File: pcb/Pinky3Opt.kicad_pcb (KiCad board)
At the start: 2 copper layers, 136 x 102.7 mm, 74 parts, among them J1 USB_C_Receptacle_USB2.0, J2 Conn_01x04, SW1 Reset, U1 ATmega32U4-A, U2 PRTR5V0U2X, Y1 16MHz

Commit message: through hole
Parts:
- added ?: Val**, kbd:M2_HOLE_v2, F.Cu at (47.6, 73.8)
- added ?: Val**, kbd:M2_HOLE_v2, F.Cu at (133.3, 92.0)
- added ?: Val**, kbd:M2_HOLE_v2, F.Cu at (47.6, 54.8)
- added Ref**: Val**, kbd:M2_HOLE_v2, F.Cu at (142.9, 50.0)
- moved D7 5.78 mm to (141.2, 43.5)
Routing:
- net /L_ROW0: track 178.2 -> 179.3 mm
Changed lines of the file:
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@@
       (net 31 "Net-(D22-A)") (pinfunction "ROW") (pintype "passive"))
   )
+  (footprint "kbd:M2_HOLE_v2" (layer "F.Cu")
+    (at 142.875 50)
+    (descr "Mounting Hole 2.2mm, no annular, M2")
+    (tags "mounting hole 2.2mm no annular m2")
+    (attr exclude_from_pos_files exclude_from_bom)
+    (fp_text reference "Ref**" (at -0.95 -0.55) (layer "F.Fab") hide
+        (effects (font (size 1 1) (thickness 0.15)))
+    )
+    (fp_text value "Val**" (at 0 0.55) (layer "F.Fab") hide
+        (effects (font (size 1 1) (thickness 0.15)))
+    )
+    (fp_text user "${REFERENCE}" (at 0.3 0) (layer "F.Fab")
+        (effects (font (size 1 1) (thickness 0.15)))
+    )
+    (pad "" np_thru_hole circle (at 0 0) (size 4.3 4.3) (drill 4.3) (layers "*.Cu" "*.Mask"))
+  )
   (footprint "kbd:ChocV1_V2_Hotswap" (layer "F.Cu")
     (at 135.255 105.41 -20)
@@
       (net 3 "+5V") (pinfunction "Pin_4") (pintype "passive"))
   )
+  (footprint "kbd:M2_HOLE_v2" (layer "F.Cu")
+    (at 47.625 73.825)
+    (descr "Mounting Hole 2.2mm, no annular, M2")
+    (tags "mounting hole 2.2mm no annular m2")
+    (attr exclude_from_pos_files exclude_from_bom)
+    (fp_text reference "" (at -0.95 -0.55) (layer "F.Fab") hide
+        (effects (font (size 1 1) (thickness 0.15)))
+    )
+    (fp_text value "Val**" (at 0 0.55) (layer "F.Fab") hide
+        (effects (font (size 1 1) (thickness 0.15)))
+    )
+    (pad "" np_thru_hole circle (at 0 0) (size 4.3 4.3) (drill 4.3) (layers "*.Cu" "*.Mask"))
+  )
   (footprint "kbd:CherryMX_Hotswap" (layer "F.Cu")
     (at 114.3 73.81875)
@@
     )
   )
+  (footprint "kbd:M2_HOLE_v2" (layer "F.Cu")
+    (at 133.35 92)
+    (descr "Mounting Hole 2.2mm, no annular, M2")
+    (tags "mounting hole 2.2mm no annular m2")
+    (attr exclude_from_pos_files exclude_from_bom)
+    (fp_text reference "" (at -0.95 -0.55) (layer "F.Fab") hide
+        (effects (font (size 1 1) (thickness 0.15)))
+    )
+    (fp_text value "Val**" (at 0 0.55) (layer "F.Fab") hide
+        (effects (font (size 1 1) (thickness 0.15)))
+    )
+    (pad "" np_thru_hole circle (at 0 0) (size 4.3 4.3) (drill 4.3) (layers "*.Cu" "*.Mask"))
+  )
   (footprint "kbd:CherryMX_Hotswap" (layer "F.Cu")
     (at 152.4 64.29375)
@@
     )
   )
+  (footprint "kbd:M2_HOLE_v2" (layer "F.Cu")
+    (at 47.625 54.775)
+    (descr "Mounting Hole 2.2mm, no annular, M2")
+    (tags "mounting hole 2.2mm no annular m2")
+    (attr exclude_from_pos_files exclude_from_bom)
+    (fp_text reference "" (at -0.95 -0.55) (layer "F.Fab") hide
+        (effects (font (size 1 1) (thickness 0.15)))
+    )
+    (fp_text value "Val**" (at 0 0.55) (layer "F.Fab") hide
+        (effects (font (size 1 1) (thickness 0.15)))
+    )
+    (pad "" np_thru_hole circle (at 0 0) (size 4.3 4.3) (drill 4.3) (layers "*.Cu" "*.Mask"))
+  )
   (footprint "kbd:CherryMX_Hotswap" (layer "F.Cu")
     (at 95.25 30.95625)
@@
   )
   (footprint "Diode_SMD:D_SOD-123" (layer "B.Cu")
-    (at 144.5 48.225 90)
+    (at 141.25 43.45 90)
     (descr "SOD-123")
     (tags "SOD-123")
@@
   (segment (start 97.425 78.0055) (end 96.225 76.8055) (width 0.254) (layer "B.Cu") (net 5))
   (segment (start 68.1 47.125) (end 62.4 47.125) (width 0.254) (layer "F.Cu") (net 6))
-  (segment (start 143.773 50.602) (end 143.773 79.277) (width 0.254) (layer "F.Cu") (net 6))
-  (segment (start 144.5 49.875) (end 143.773 50.602) (width 0.254) (layer "F.Cu") (net 6))
+  (segment (start 140.298 46.052) (end 140.298 51.067429) (width 0.254) (layer "F.Cu") (net 6))
+  (segment (start 140.298 51.067429) (end 143.773 54.542429) (width 0.254) (layer "F.Cu") (net 6))
+  (segment (start 141.25 45.1) (end 140.298 46.052) (width 0.254) (layer "F.Cu") (net 6))
   (segment (start 143.773 79.277) (end 139.275 83.775) (width 0.254) (layer "F.Cu") (net 6))
-  (via (at 144.5 49.875) (size 0.8) (drill 0.4) (layers "F.Cu" "B.Cu") (net 6))
+  (segment (start 143.773 54.542429) (end 143.773 79.277) (width 0.254) (layer "F.Cu") (net 6))
   (via (at 139.275 83.775) (size 0.8) (drill 0.4) (layers "F.Cu" "B.Cu") (net 6))
   (via (at 68.1 47.125) (size 0.8) (drill 0.4) (layers "F.Cu" "B.Cu") (net 6))
+  (via (at 141.25 45.1) (size 0.8) (drill 0.4) (layers "F.Cu" "B.Cu") (net 6))
   (via (at 62.4 47.125) (size 0.8) (drill 0.4) (layers "F.Cu" "B.Cu") (net 6))
-  (segment (start 130.225 49.875) (end 125.45 45.1) (width 0.254) (layer "B.Cu") (net 6))
   (segment (start 122.2 45.1) (end 117.45 40.35) (width 0.254) (layer "B.Cu") (net 6))
   (segment (start 87.35 40.35) (end 84.1 40.35) (width 0.254) (layer "B.Cu") (net 6))
@@
   (segment (start 139.275 83.775) (end 139.27325 83.77675) (width 0.254) (layer "B.Cu") (net 6))
   (segment (start 139.27325 83.77675) (end 105.76725 83.77675) (width 0.254) (layer "B.Cu") (net 6))
-  (segment (start 144.5 49.875) (end 130.225 49.875) (width 0.254) (layer "B.Cu") (net 6))
+  (segment (start 125.45 45.1) (end 141.25 45.1) (width 0.254) (layer "B.Cu") (net 6))
   (segment (start 74.875 40.35) (end 68.1 47.125) (width 0.254) (layer "B.Cu") (net 6))
   (segment (start 117.45 40.35) (end 87.35 40.35) (width 0.254) (layer "B.Cu") (net 6))
@@
   (segment (start 137.103 37.49025) (end 137.103 40.160546) (width 0.254) (layer "B.Cu") (net 12))
   (segment (start 126.55825 42.90825) (end 125.45 41.8) (width 0.254) (layer "B.Cu") (net 12))
-  (segment (start 156.153 44.923046) (end 153.405296 47.67075) (width 0.254) (layer "B.Cu") (net 13))
-  (segment (start 158.242 40.16375) (end 156.153 42.25275) (width 0.254) (layer "B.Cu") (net 13))
-  (segment (start 153.405296 47.67075) (end 145.59575 47.67075) (width 0.254) (layer "B.Cu") (net 13))
-  (segment (start 156.153 42.25275) (end 156.153 44.923046) (width 0.254) (layer "B.Cu") (net 13))
-  (segment (start 145.59575 47.67075) (end 144.5 46.575) (width 0.254) (layer "B.Cu") (net 13))
+  (segment (start 158.242 40.16375) (end 156.365 38.28675) (width 0.254) (layer "B.Cu") (net 13))
+  (segment (start 156.365 38.28675) (end 144.76325 38.28675) (width 0.254) (layer "B.Cu") (net 13))
+  (segment (start 144.76325 38.28675) (end 141.25 41.8) (width 0.254) (layer "B.Cu") (net 13))
   (segment (start 144.5 68.925) (end 144.5 79.578134) (width 0.254) (layer "F.Cu") (net 14))
   (segment (start 144.5 79.578134) (end 139.576134 84.502) (width 0.254) (layer "F.Cu") (net 14))
@@
   (segment (start 83.05 91.675) (end 87.778235 91.675) (width 0.254) (layer "B.Cu") (net 35))
   (segment (start 55.854012 89.004423) (end 81.542427 89.004423) (width 0.254) (layer "F.Cu") (net 36))
+  (segment (start 50.202 61.648) (end 50.075 61.775) (width 0.254) (layer "F.Cu") (net 36))
+  (segment (start 50.075 42.725) (end 50.202 42.852) (width 0.254) (layer "F.Cu") (net 36))
+  (segment (start 50.202 42.852) (end 50.202 61.648) (width 0.254) (layer "F.Cu") (net 36))
   (segment (start 50.075 83.225411) (end 55.854012 89.004423) (width 0.254) (layer "F.Cu") (net 36))
-  (segment (start 50.075 80.8) (end 50.075 61.775) (width 0.254) (layer "F.Cu") (net 36))
+  (segment (start 50.202 80.673) (end 50.075 80.8) (width 0.254) (layer "F.Cu") (net 36))
+  (segment (start 50.075 61.775) (end 50.202 61.902) (width 0.254) (layer "F.Cu") (net 36))
   (segment (start 50.075 80.8) (end 50.075 83.225411) (width 0.254) (layer "F.Cu") (net 36))
-  (segment (start 50.075 61.775) (end 50.075 42.725) (width 0.254) (layer "F.Cu") (net 36))
+  (segment (start 50.202 61.902) (end 50.202 80.673) (width 0.254) (layer "F.Cu") (net 36))
   (via (at 50.075 61.775) (size 0.8) (drill 0.4) (layers "F.Cu" "B.Cu") (net 36))
   (via (at 50.075 42.725) (size 0.8) (drill 0.4) (layers "F.Cu" "B.Cu") (net 36))
@@
   (segment (start 146.831678 87.057531) (end 142.853989 91.03522) (width 0.254) (layer "F.Cu") (net 41))
   (segment (start 145.315 84.31) (end 145.3 84.325) (width 0.254) (layer "F.Cu") (net 41))
+  (segment (start 145.452 61.61675) (end 145.315 61.75375) (width 0.254) (layer "F.Cu") (net 41))
   (segment (start 145.315 84.265) (end 145.325 84.275) (width 0.254) (layer "F.Cu") (net 41))
   (segment (start 145.325 84.275) (end 145.315 84.285) (width 0.254) (layer "F.Cu") (net 41))
   (segment (start 142.853989 91.03522) (end 142.853989 112.211294) (width 0.254) (layer "F.Cu") (net 41))
   (segment (start 145.3 84.325) (end 145.315 84.34) (width 0.254) (layer "F.Cu") (net 41))
+  (segment (start 145.452 42.827) (end 145.452 61.61675) (width 0.254) (layer "F.Cu") (net 41))
+  (segment (start 145.325 42.7) (end 145.452 42.827) (width 0.254) (layer "F.Cu") (net 41))
   (segment (start 145.315 85.540853) (end 146.831678 87.057531) (width 0.254) (layer "F.Cu") (net 41))
   (segment (start 145.315 84.285) (end 145.315 84.31) (width 0.254) (layer "F.Cu") (net 41))
-  (segment (start 145.315 42.71) (end 145.315 61.75375) (width 0.254) (layer "F.Cu") (net 41))
   (segment (start 145.315 61.75375) (end 145.315 84.265) (width 0.254) (layer "F.Cu") (net 41))
   (via (at 145.315 61.75375) (size 0.8) (drill 0.4) (layers "F.Cu" "B.Cu") (net 41))

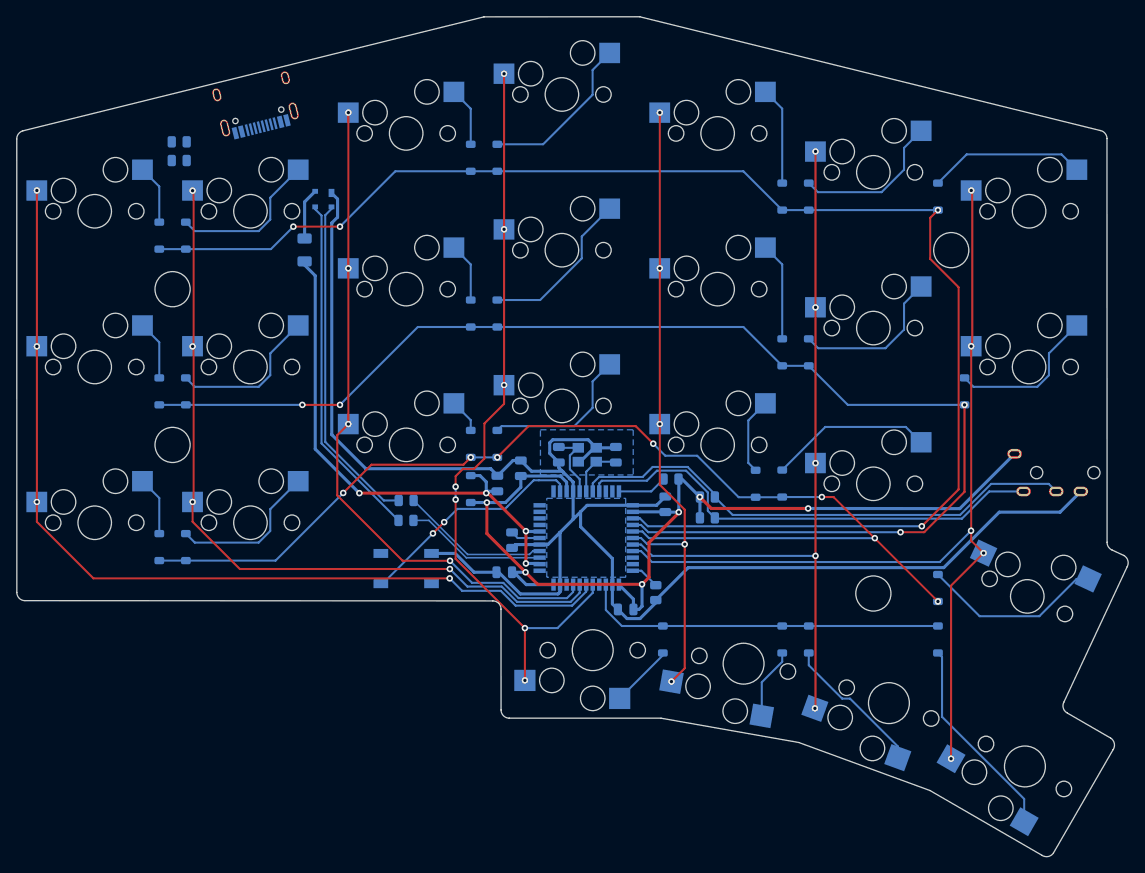
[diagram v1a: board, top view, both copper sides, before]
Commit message: socket pad via
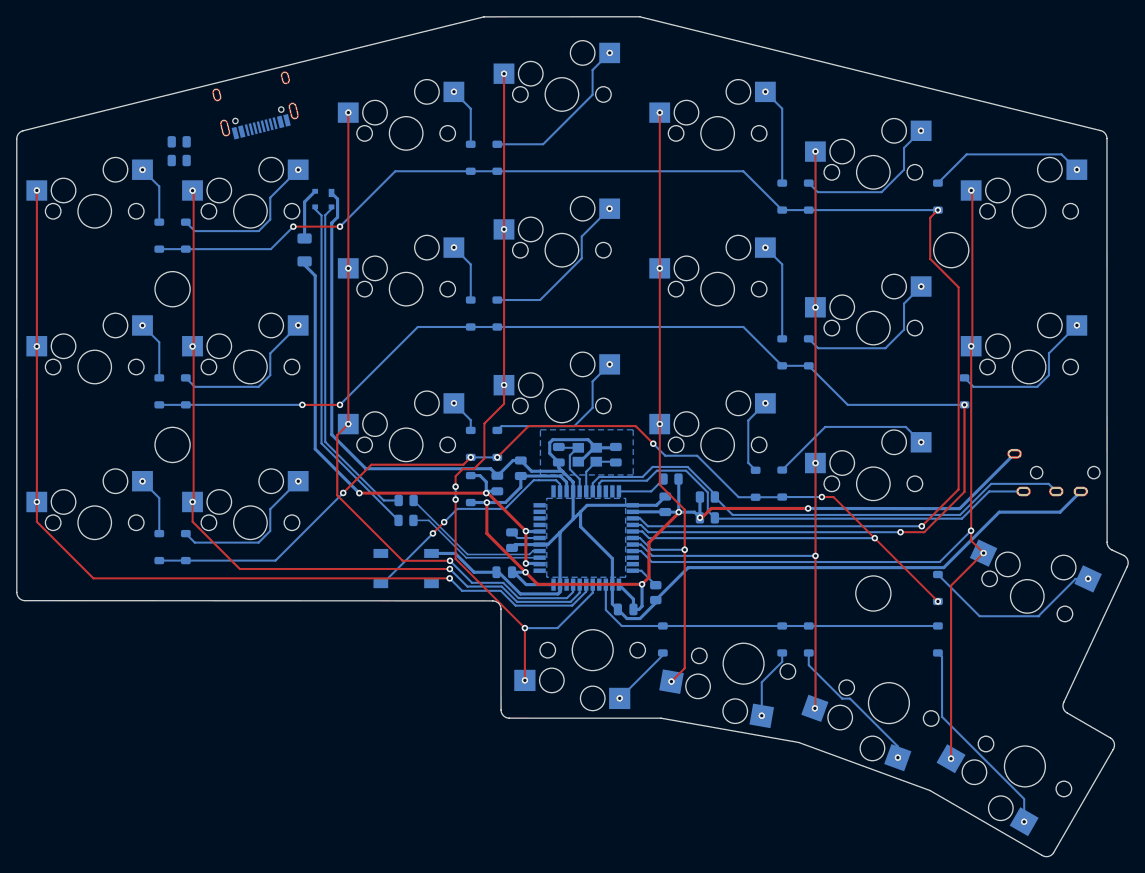
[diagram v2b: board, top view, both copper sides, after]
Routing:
- net +5V: track 124.2 -> 123.3 mm
- net Net-(D21-A): track 22.4 -> 22.5 mm, vias 0 -> 1
- net Net-(D5-A): track 12.0 -> 12.1 mm, vias 0 -> 1
- net Net-(D17-A): track 4.16 -> 4.24 mm, vias 0 -> 1
- net Net-(D10-A): track 7.26 -> 7.34 mm, vias 0 -> 1
- net Net-(D3-A): track 7.26 -> 7.34 mm, vias 0 -> 1
- net Net-(D14-A): vias 0 -> 1
- net Net-(D19-A): track 9.42 -> 9.47 mm, vias 0 -> 1
- net Net-(D9-A): vias 0 -> 1
- net Net-(D7-A): track 19.2 -> 19.3 mm, vias 0 -> 1
- net Net-(D2-A): vias 0 -> 1
- net Net-(D16-A): vias 0 -> 1
- net Net-(D20-A): vias 0 -> 1
- net Net-(D18-A): vias 0 -> 1
- net Net-(D4-A): track 20.1 -> 20.2 mm, vias 0 -> 1
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
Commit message: maybe done left hand
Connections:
- net /HDETECT renamed /HDETECT_L
- net /L_COL0 renamed /COL0_L
- net /L_COL1 renamed /COL1_L
- net /L_COL2 renamed /COL2_L
- net /L_COL3 renamed /COL3_L
- net /L_COL4 renamed /COL4_L
- net /L_COL5 renamed /COL5_L
- net /L_COL6 renamed /COL6_L
- net /L_ROW0 renamed /ROW0_L
- net /L_ROW1 renamed /ROW1_L
- net /L_ROW2 renamed /ROW2_L
- net /L_ROW3 renamed /ROW3_L
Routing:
- net GND: track 209.5 -> 254.0 mm
- net VCC: track 6.31 -> 26.3 mm, vias 0 -> 2
- net Net-(U2-IO2): track 42.6 -> 62.2 mm
- net Net-(U2-IO1): track 41.0 -> 60.0 mm
- net Net-(J1-CC2): track 0.00 -> 14.1 mm, vias 0 -> 2
- net Net-(J1-CC1): track 0.00 -> 10.7 mm, vias 0 -> 2
